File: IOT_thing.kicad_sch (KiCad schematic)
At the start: 64 parts, among them J1 USB_C_Receptacle_USB2.0_16P, J2 Conn_01x04, J3 Screw_Terminal_01x03, J4 Screw_Terminal_01x08, J5 Screw_Terminal_01x02, J6 Conn_02x05_Odd_Even, K1 RT314A05, Q1 UMH3N, Q2 UMH3N, Q3 BC817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

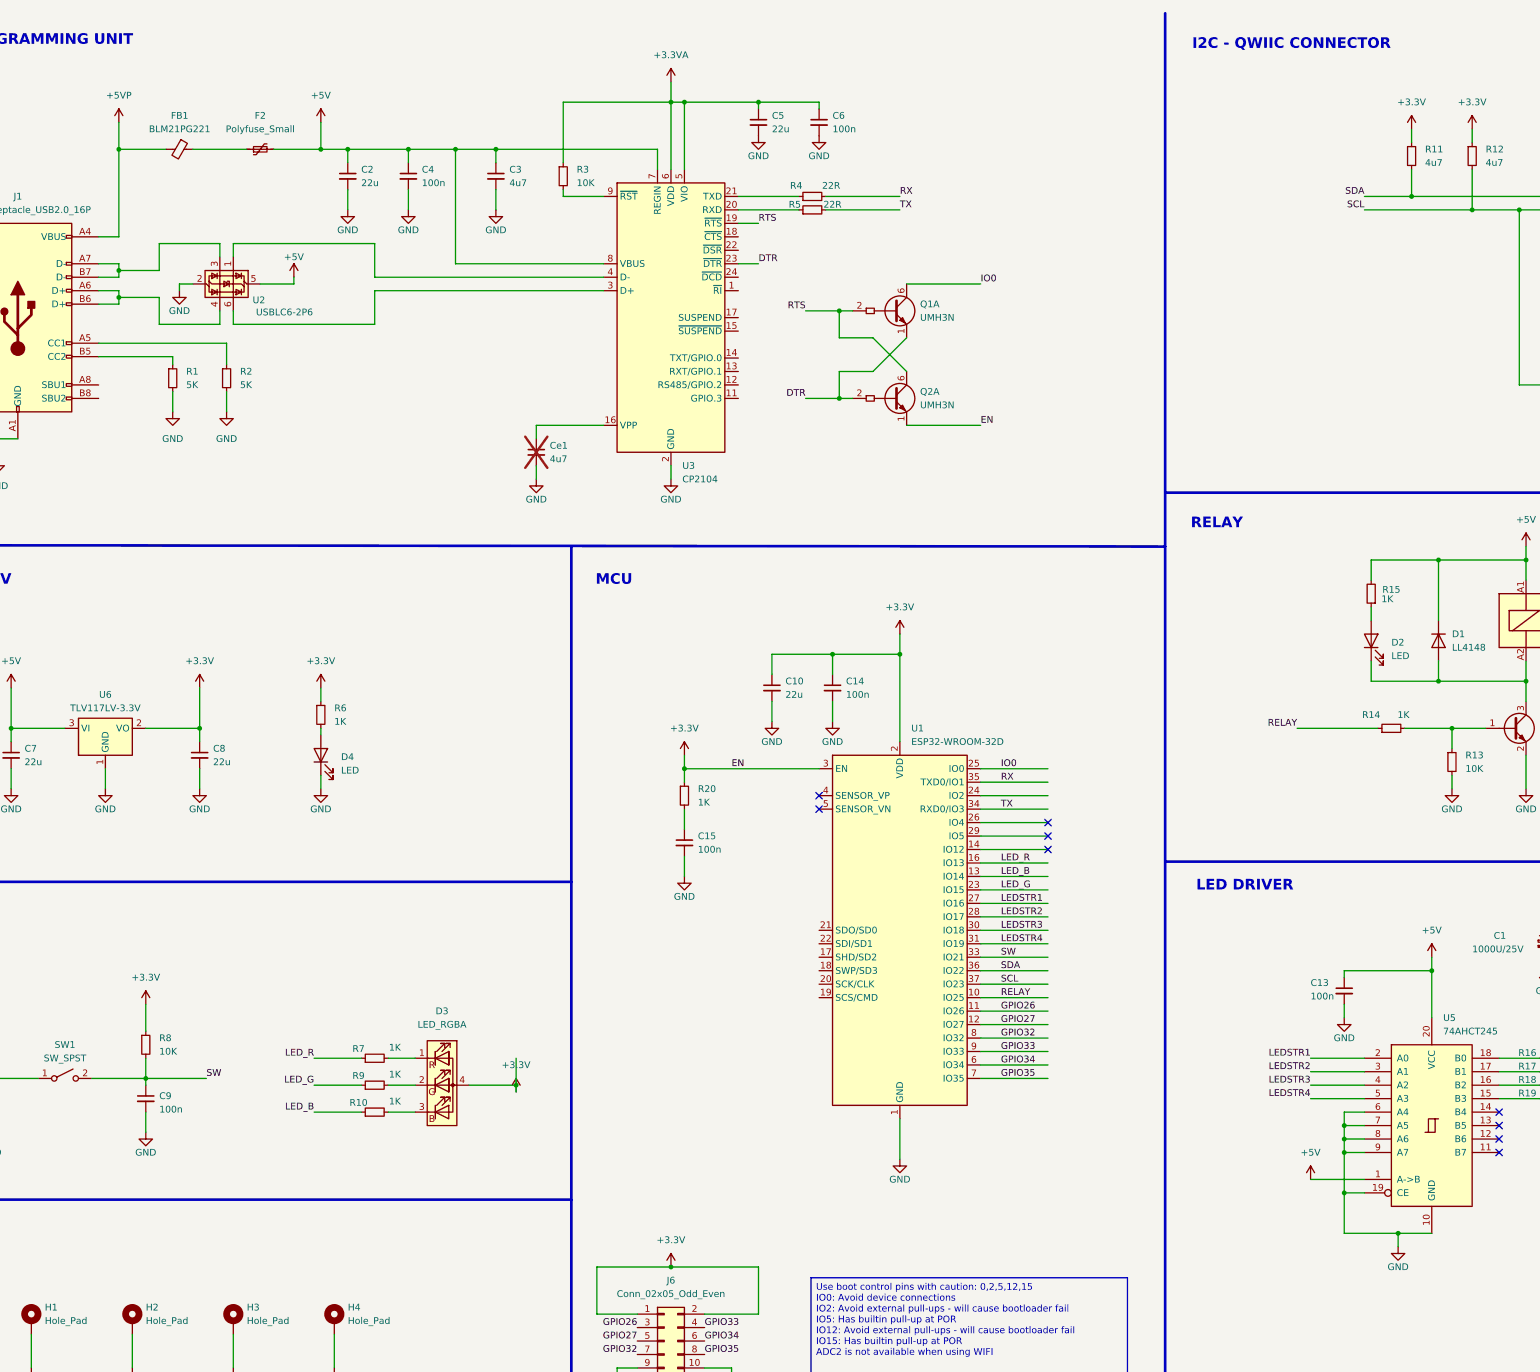
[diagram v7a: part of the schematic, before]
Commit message: Started laying out the components
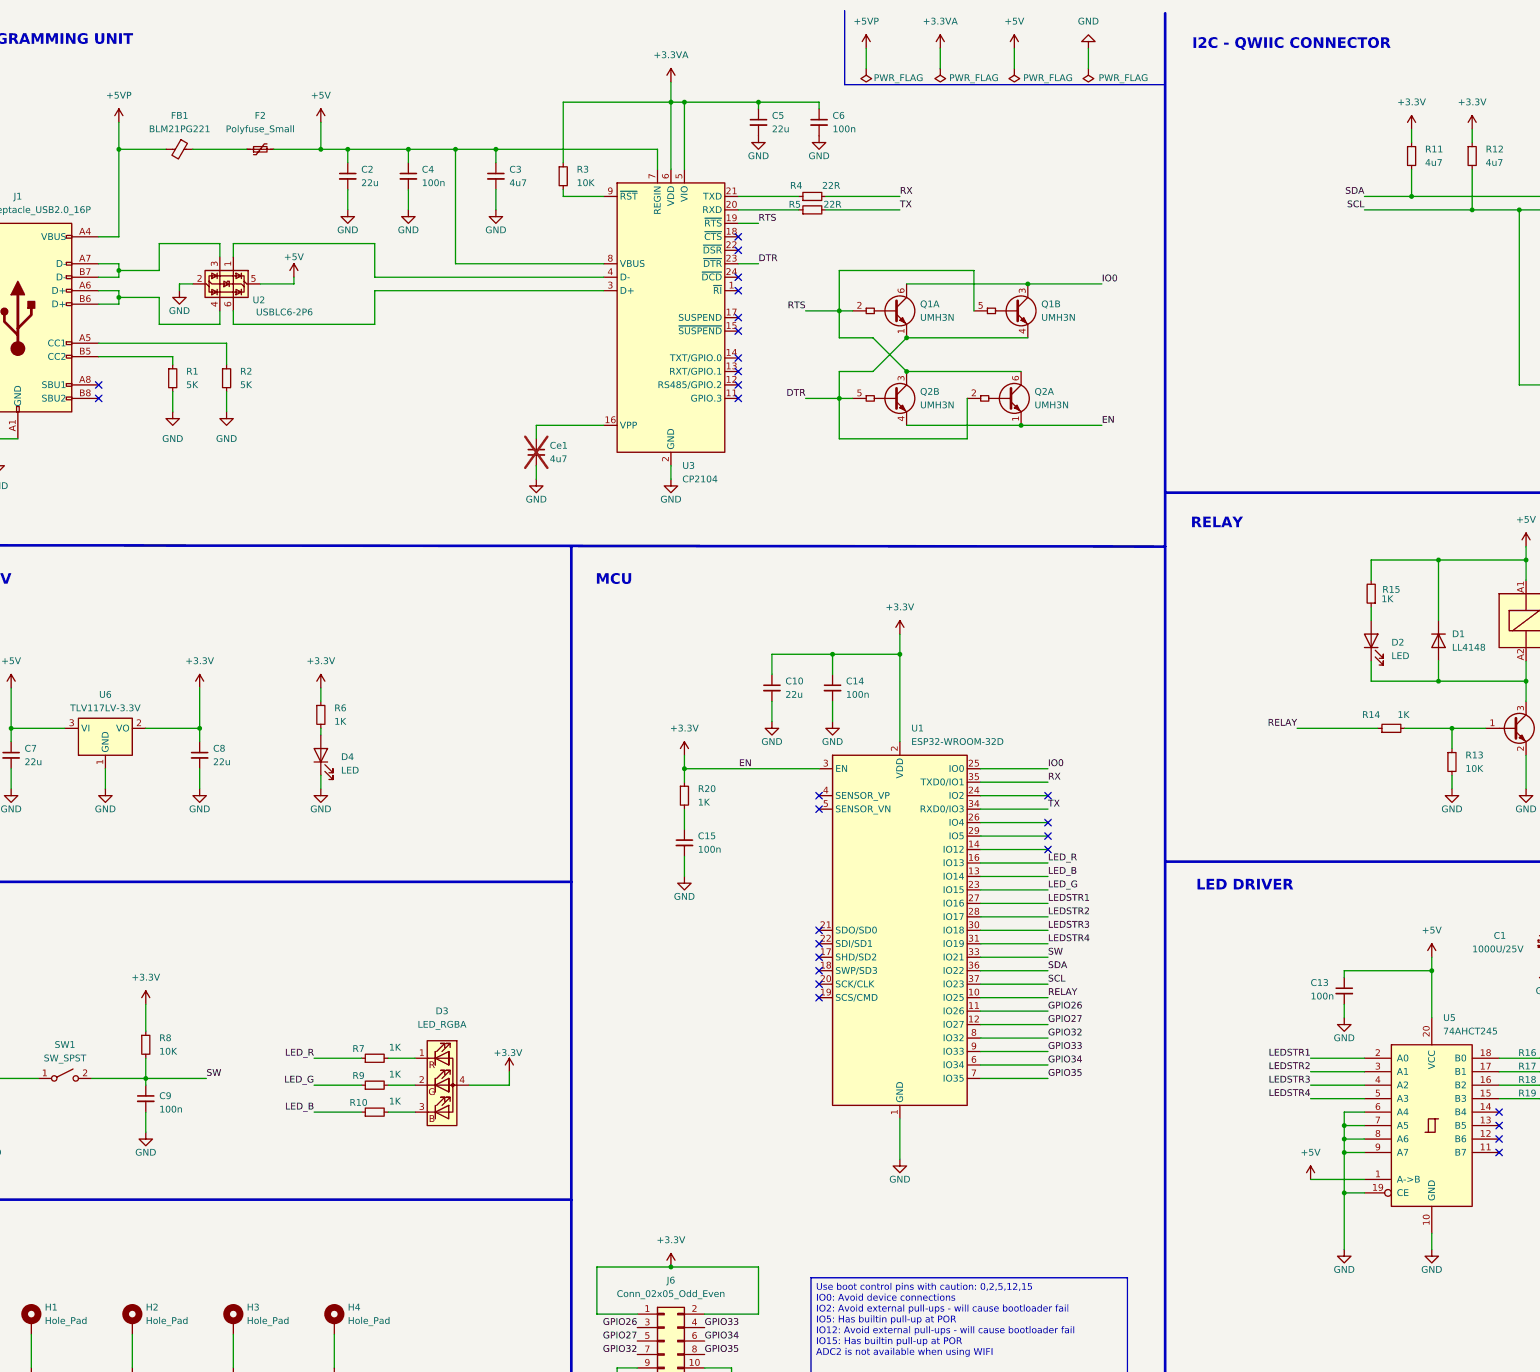
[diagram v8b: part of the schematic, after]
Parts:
- added unit 2 of Q1
- added unit 1 of Q2
- C10, C11, C2, C5, C7, C8: footprint Capacitor_THT:CP_Radial_D10.0mm_P5.00mm -> Capacitor_SMD:C_0805_2012Metric_Pad1.18x1.45mm_HandSolder
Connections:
- net +3.3V: now also Q2.4 (E2), Q2.1 (E1); no longer Q2.1 (E1)
- net DTR: now also Q2.5 (B2), Q1.4 (E2), Q2.2 (B1); no longer Q2.2 (B1)
- net IO0: now also Q1.3 (C2)
- net RTS: now also Q2.3 (C2), Q1.5 (B2), Q2.6 (C1); no longer Q2.6 (C1)
- no-connect marks 9 -> 28
